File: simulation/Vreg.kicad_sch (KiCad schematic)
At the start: 7 parts, among them U101 LM317_TO-220

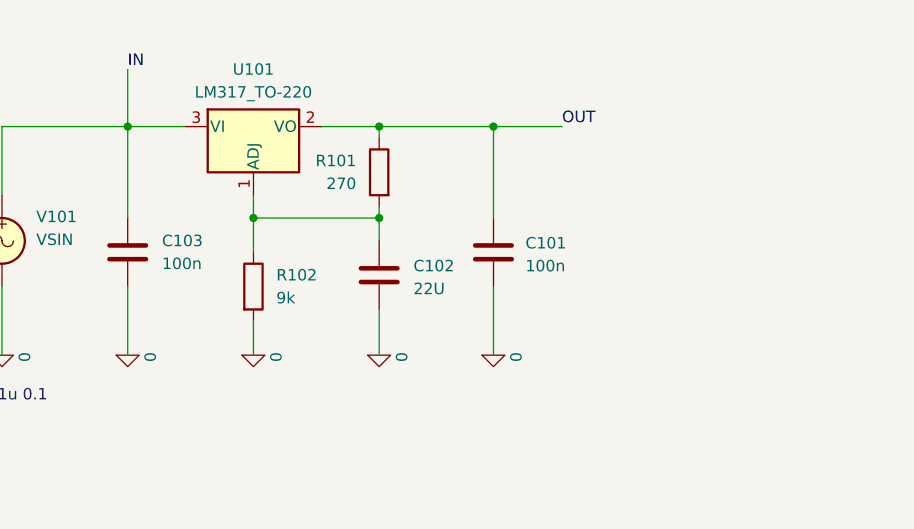
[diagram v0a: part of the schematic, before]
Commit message: Added load to voltage regulator simulation
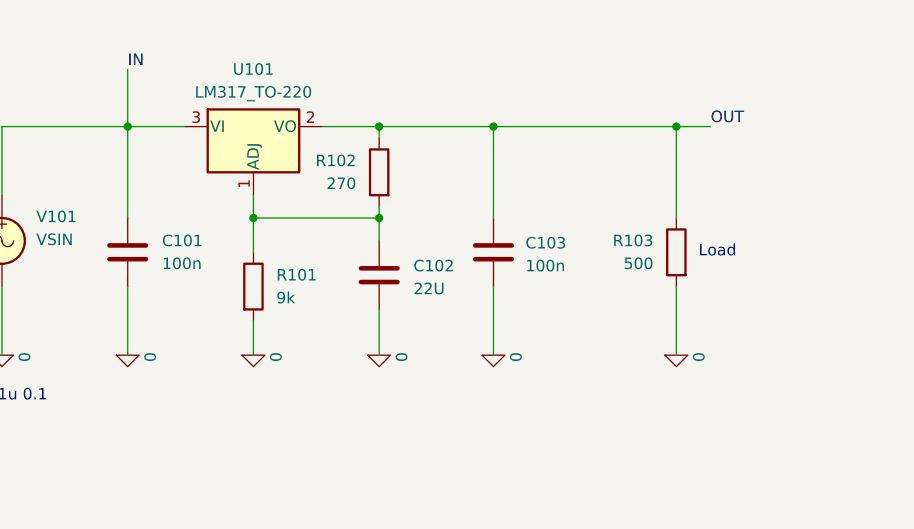
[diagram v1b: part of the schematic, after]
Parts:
- added R103: 500, symbol Device:R
- renumbered C103 to C101, C101 to C103, R102 to R101, R101 to R102
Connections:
- net 0: now also R103.2
- net OUT: now also R103.1
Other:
- note added: "Load"
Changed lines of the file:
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@@
+		)
+	)
+	(text "Load"
+		(exclude_from_sim no)
+		(at 197.612 102.87 0)
+		(effects
+			(font
+				(size 1.27 1.27)
+			)
 		)
 	)
@@
 	)
 	(junction
+		(at 193.04 88.9)
+		(diameter 0)
+		(color 0 0 0 0)
+	)
+	(junction
 		(at 172.72 88.9)
 		(diameter 0)
@@
 	(wire
 		(pts
+			(xy 193.04 88.9) (xy 196.85 88.9)
+		)
+		(stroke
+			(width 0)
+			(type default)
+		)
+	)
+	(wire
+		(pts
 			(xy 146.05 99.06) (xy 146.05 102.87)
 		)
@@
 	(wire
 		(pts
+			(xy 193.04 88.9) (xy 193.04 99.06)
+		)
+		(stroke
+			(width 0)
+			(type default)
+		)
+	)
+	(wire
+		(pts
 			(xy 160.02 109.22) (xy 160.02 114.3)
 		)
@@
 	(wire
 		(pts
-			(xy 172.72 88.9) (xy 180.34 88.9)
+			(xy 172.72 88.9) (xy 193.04 88.9)
 		)
 		(stroke
@@
 	(wire
 		(pts
+			(xy 193.04 106.68) (xy 193.04 114.3)
+		)
+		(stroke
+			(width 0)
+			(type default)
+		)
+	)
+	(wire
+		(pts
 			(xy 118.11 106.68) (xy 118.11 114.3)
 		)
@@
 	)
 	(label "OUT"
-		(at 180.34 88.9 0)
+		(at 196.85 88.9 0)
 		(effects
 			(font
@@
 		(dnp no)
 		(fields_autoplaced yes)
-		(property "Reference" "C103"
+		(property "Reference" "C101"
 			(at 135.89 101.5999 0)
 			(effects
@@
 			(project "Vreg"
 				(path "/9048a61a-cc24-400a-9e00-8ca96074b3d2"
-					(reference "C103")
+					(reference "C101")
 					(unit 1)
 				)
@@
 		(on_board yes)
 		(dnp no)
-		(property "Reference" "#GND0101"
+		(property "Reference" "#GND0103"
 			(at 146.05 116.84 0)
 			(effects
@@
 			(project "Blocking"
 				(path "/9048a61a-cc24-400a-9e00-8ca96074b3d2"
-					(reference "#GND0101")
+					(reference "#GND0103")
 					(unit 1)
 				)
@@
 		(on_board yes)
 		(dnp no)
-		(property "Reference" "#GND0102"
+		(property "Reference" "#GND0101"
 			(at 118.11 116.84 0)
 			(effects
@@
 			(project "Blocking"
 				(path "/9048a61a-cc24-400a-9e00-8ca96074b3d2"
-					(reference "#GND0102")
+					(reference "#GND0101")
+					(unit 1)
+				)
+			)
+		)
+	)
+	(symbol
+		(lib_id "pspice:0")
+		(at 193.04 114.3 0)
+		(unit 1)
+		(exclude_from_sim no)
+		(in_bom yes)
+		(on_board yes)
+		(dnp no)
+		(property "Reference" "#GND0106"
+			(at 193.04 116.84 0)
+			(effects
+				(font
+					(size 1.27 1.27)
+				)
+				(hide yes)
+			)
+		)
+		(property "Value" "0"
+			(at 195.58 115.062 90)
+			(effects
+				(font
+					(size 1.27 1.27)
+				)
+				(justify left)
+			)
+		)
+		(property "Footprint" ""
+			(at 193.04 114.3 0)
+			(effects
+				(font
+					(size 1.27 1.27)
+				)
+				(hide yes)
+			)
+		)
+		(property "Datasheet" "~"
+			(at 193.04 114.3 0)
+			(effects
+				(font
+					(size 1.27 1.27)
+				)
+				(hide yes)
+			)
+		)
+		(property "Description" ""
+			(at 193.04 114.3 0)
+			(effects
+				(font
+					(size 1.27 1.27)
+				)
+				(hide yes)
+			)
+		)
+		(pin "1"
+		)
+		(instances
+			(project "Vreg"
+				(path "/9048a61a-cc24-400a-9e00-8ca96074b3d2"
+					(reference "#GND0106")
 					(unit 1)
 				)
@@
 		(on_board yes)
 		(dnp no)
-		(property "Reference" "#GND0105"
+		(property "Reference" "#GND0104"
 			(at 160.02 116.84 0)
 			(effects
@@
 			(project "Vreg"
 				(path "/9048a61a-cc24-400a-9e00-8ca96074b3d2"
-					(reference "#GND0105")
+					(reference "#GND0104")
 					(unit 1)
 				)
@@
 		(dnp no)
 		(fields_autoplaced yes)
-		(property "Reference" "R102"
+		(property "Reference" "R101"
 			(at 148.59 105.4099 0)
 			(effects
@@
 			(project "Vreg"
 				(path "/9048a61a-cc24-400a-9e00-8ca96074b3d2"
-					(reference "R102")
+					(reference "R101")
 					(unit 1)
 				)
@@
 		(on_board yes)
 		(dnp no)
-		(property "Reference" "#GND0104"
+		(property "Reference" "#GND0105"
 			(at 172.72 116.84 0)
 			(effects
@@
 			(project "Vreg"
 				(path "/9048a61a-cc24-400a-9e00-8ca96074b3d2"
-					(reference "#GND0104")
+					(reference "#GND0105")
 					(unit 1)
 				)
@@
 		(on_board yes)
 		(dnp no)
-		(property "Reference" "C101"
+		(property "Reference" "C103"
 			(at 176.276 101.854 0)
 			(effects
@@
 			(project ""
 				(path "/9048a61a-cc24-400a-9e00-8ca96074b3d2"
-					(reference "C101")
+					(reference "C103")
 					(unit 1)
 				)
@@
 		(on_board yes)
 		(dnp no)
-		(property "Reference" "R101"
+		(property "Reference" "R102"
 			(at 157.48 92.7099 0)
 			(effects
@@
 			(project ""
 				(path "/9048a61a-cc24-400a-9e00-8ca96074b3d2"
-					(reference "R101")
+					(reference "R102")
+					(unit 1)
+				)
+			)
+		)
+	)
+	(symbol
+		(lib_id "Device:R")
+		(at 193.04 102.87 0)
+		(mirror y)
+		(unit 1)
+		(exclude_from_sim no)
+		(in_bom yes)
+		(on_board yes)
+		(dnp no)
+		(property "Reference" "R103"
+			(at 190.5 101.5999 0)
+			(effects
+				(font
+					(size 1.27 1.27)
+				)
+				(justify left)
+			)
+		)
+		(property "Value" "500"
+			(at 190.5 104.1399 0)
+			(effects
+				(font
+					(size 1.27 1.27)
+				)
+				(justify left)
+			)
+		)
+		(property "Footprint" ""
+			(at 194.818 102.87 90)
+			(effects
+				(font
+					(size 1.27 1.27)
+				)
+				(hide yes)
+			)
+		)
+		(property "Datasheet" "~"
+			(at 193.04 102.87 0)
+			(effects
+				(font
+					(size 1.27 1.27)
+				)
+				(hide yes)
+			)
+		)
+		(property "Description" "Resistor"
+			(at 193.04 102.87 0)
+			(effects
+				(font
+					(size 1.27 1.27)
+				)
+				(hide yes)
+			)
+		)
+		(pin "2"
+		)
+		(pin "1"
+		)
+		(instances
+			(project "Vreg"
+				(path "/9048a61a-cc24-400a-9e00-8ca96074b3d2"
+					(reference "R103")
 					(unit 1)
 				)
@@
 		(on_board yes)
 		(dnp no)
-		(property "Reference" "#GND0103"
+		(property "Reference" "#GND0102"
 			(at 132.08 116.84 0)
 			(effects
@@
 			(project "Vreg"
 				(path "/9048a61a-cc24-400a-9e00-8ca96074b3d2"
-					(reference "#GND0103")
-					(unit 1)
-				)
+					(reference "#GND0102")
+					(unit 1)
+				)
